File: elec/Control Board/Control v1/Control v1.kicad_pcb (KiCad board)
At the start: 2 copper layers, 126.3 x 160 mm, 175 parts, among them J10 Conn_02x12_Odd_Even, J103 Screw_Terminal_01x02, J106 Conn_01x04, J107 Conn_01x07, J11 Screw_Terminal_01x02, J111 Conn_01x08, J15 DB25_Female_MountingHoles, J16 Conn_01x04, J17 Conn_01x05, J18 Conn_01x04, J19 Conn_01x07, J2 DB9_Female_MountingHoles, J20 Screw_Terminal_01x02, J201 0.100_2Pin, J202 Conn_01x04, J21 Conn_01x04_Pin, J23 0.100_2Pin, J24 0.100_2Pin, J25 Conn_01x04, J3 Conn_01x08, J301 RJ12_6P6C_HORZ, J302 0.100_2Pin, J4 Conn_01x08, J5 Conn_01x08, J6 Conn_01x08, J7 Conn_01x08, J8 Conn_02x18_Odd_Even, J9 Conn_01x10_MountingPin, Q1 BSS138, Q10 BSS138, Q2 NCE01P30K, Q201 BSS138, Q202 BSS138, Q3 BSS138, Q301 BSS138, Q302 BSS138, Q303 BSS138, Q304 BSS138, Q4 BSS138, Q5 BSS138, Q6 BSS138, Q7 BSS138, Q8 BSS138, Q9 BSS138, SW101 SW_DIP_x08

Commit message: Add footrpint to Max31850 module.
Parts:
- removed J10: Conn_02x12_Odd_Even, Connector_PinHeader_2.00mm:PinHeader_2x12_P2.00mm_Vertical
- removed J301: RJ12_6P6C_HORZ, PubInv_PCB:RJ12_Amphenol_54601
- removed R102: DNI, Resistor_SMD:R_0603_1608Metric_Pad0.98x0.95mm_HandSolder
- removed SW101: SW_DIP_x08, PubInv_PCB:SMDIP-16_L11.39_W6.7mm
- added D2: DNI, Diode_SMD:D_MiniMELF, F.Cu at (70.0, 63.6)
- added J14: Conn_01x04, Connector_PinHeader_2.54mm:PinHeader_1x04_P2.54mm_Vertical, F.Cu at (61.2, 62.5)
- added J15: Conn_01x05, Connector_PinHeader_2.54mm:PinHeader_1x05_P2.54mm_Vertical, F.Cu at (75.8, 78.4)
- added J2: Conn_01x08, Connector_PinSocket_2.54mm:PinSocket_1x08_P2.54mm_Vertical, F.Cu at (159.0, 88.9)
- added J22: Conn_01x04, Connector_PinHeader_2.54mm:PinHeader_1x04_P2.54mm_Vertical, F.Cu at (43.4, 127.0)
- added JP1: Breakout, PubInv_KiCad_PCB:Adafruit_MAX31850K_Module, F.Cu at (222.5, 44.5)
- added JP2: Breakout, PubInv_KiCad_PCB:Adafruit_MAX31850K_Module, F.Cu at (222.5, 66.4)
- added JP3: Breakout, PubInv_KiCad_PCB:Adafruit_MAX31850K_Module, F.Cu at (222.5, 88.4)
- added JP6: SolderJumper_3_Bridged12, Jumper:SolderJumper-3_P1.3mm_Bridged12_RoundedPad1.0x1.5mm, F.Cu at (194.3, 34.9)
- added JP7: SolderJumper_3_Bridged12, Jumper:SolderJumper-3_P1.3mm_Bridged12_RoundedPad1.0x1.5mm, F.Cu at (194.3, 38.8)
- added JP8: SolderJumper_3_Bridged12, Jumper:SolderJumper-3_P1.3mm_Bridged12_RoundedPad1.0x1.5mm, F.Cu at (194.3, 42.6)
- added JP9: SolderJumper_3_Bridged12, Jumper:SolderJumper-3_P1.3mm_Bridged12_RoundedPad1.0x1.5mm, F.Cu at (194.9, 49.0)
- added R11: DNI, Resistor_SMD:R_0603_1608Metric_Pad0.98x0.95mm_HandSolder, F.Cu at (49.5, 91.0)
- added R15: 1K, Resistor_SMD:R_0603_1608Metric_Pad0.98x0.95mm_HandSolder, F.Cu at (65.6, 86.8)
- added R17: 1K, Resistor_SMD:R_0603_1608Metric_Pad0.98x0.95mm_HandSolder, F.Cu at (74.3, 85.6)
- added R51: 39R, Resistor_SMD:R_0603_1608Metric_Pad0.98x0.95mm_HandSolder, F.Cu at (22.7, 121.5)
- added R52: 1R, Resistor_SMD:R_0603_1608Metric_Pad0.98x0.95mm_HandSolder, F.Cu at (22.7, 124.0)
- added R53: DNI, Resistor_SMD:R_0603_1608Metric_Pad0.98x0.95mm_HandSolder, F.Cu at (22.7, 126.5)
- added R54: DNI, Resistor_SMD:R_0603_1608Metric_Pad0.98x0.95mm_HandSolder, F.Cu at (22.7, 129.0)
- added TP10: +VccMAX31850_1, TestPoint:TestPoint_Loop_D2.54mm_Drill1.5mm_Beaded, F.Cu at (245.1, 27.4)
- added TP9: SDA_5V, TestPoint:TestPoint_Loop_D2.54mm_Drill1.5mm_Beaded, F.Cu at (27.4, 122.7)
- J17: value Conn_01x05 -> Conn_01x07; footprint Connector_PinHeader_2.54mm:PinHeader_1x05_P2.54mm_Vertical -> Connector_PinHeader_2.54mm:PinHeader_1x07_P2.54mm_Vertical
- J18: value Conn_01x04 -> Conn_01x04_Pin
- J19: value Conn_01x07 -> RJ12_6P6C_HORZ; footprint Connector_PinHeader_2.54mm:PinHeader_1x07_P2.54mm_Vertical -> PubInv_KiCad_PCB:RJ12_Amphenol_54601
- J20: value Screw_Terminal_01x02 -> 0.100_2Pin; footprint TerminalBlock_MetzConnect:TerminalBlock_MetzConnect_Type073_RT02602HBLU_1x02_P5.08mm_Horizontal -> Connector_PinHeader_2.54mm:PinHeader_1x02_P2.54mm_Vertical
- J21: value Conn_01x04_Pin -> 0.100_2Pin; footprint Connector_PinHeader_2.54mm:PinHeader_1x04_P2.54mm_Vertical -> Connector_PinHeader_2.54mm:PinHeader_1x02_P2.54mm_Vertical
- J4: footprint Connector_PinSocket_2.54mm:PinSocket_1x08_P2.54mm_Vertical -> Connector_PinHeader_2.54mm:PinHeader_1x08_P2.54mm_Vertical
- J7: value Conn_01x08 -> Conn_02x18_Odd_Even; footprint Connector_PinSocket_2.54mm:PinSocket_1x08_P2.54mm_Vertical -> Connector_PinSocket_2.54mm:PinSocket_2x18_P2.54mm_Vertical
- J8: value Conn_02x18_Odd_Even -> Conn_01x10_MountingPin; footprint Connector_PinSocket_2.54mm:PinSocket_2x18_P2.54mm_Vertical -> Connector_PinSocket_2.54mm:PinSocket_1x10_P2.54mm_Vertical
- J9: value Conn_01x10_MountingPin -> Conn_02x12_Odd_Even; footprint Connector_PinSocket_2.54mm:PinSocket_1x10_P2.54mm_Vertical -> Connector_PinHeader_2.00mm:PinHeader_2x12_P2.00mm_Vertical
- R10, R27, R4, R5: value DNI -> 1R0
- R12: value 1K -> 1R0
- R13, R22, R32: value 1K -> DNI
- R18: value 10K -> 10k
- R19: value 1K -> 10k
- R20: value 1K -> 10K
- R21, R36: value 10K -> 1K
- R23: value 1R0 -> 10K
- R24, R41: value 1R -> 1K
- R25, R48: value 1R -> 10K
- R26, R6, R7, R8: value DNI -> 1K
- R28, R38: value DNI -> 1R
- R29: value 1K -> 1R
- R31, R39, R42: value 10K -> DNI
- R34: value 1R -> DNI
- R35, R49: value DNI -> 10K
- R45: value 10K -> 1R
- R46, R47: value 39R -> 10K
- R50: value DNI -> 39R
- R9: value 1R0 -> 1K
- TP1: value ControllerVCC -> +VccMAX31850
- TP2: value CPIO -> ControllerVCC
- TP3: value SCK -> CPIO
- TP4: value COPI -> SCK
- TP5: value nCS -> COPI
- TP6: value I2C_VCC -> nCS
- TP7: value SCL_5V -> I2C_VCC
- TP8: value SDA_5V -> SCL_5V
- moved D1 172.5 mm to (69.6, 83.2)
- moved R23 170.4 mm to (77.9, 58.0)
- moved R22 166.8 mm to (82.7, 91.0)
- moved Q1 166.8 mm to (70.4, 88.2)
- moved R25 165.0 mm to (84.7, 60.4), turned to 180 degrees
- moved R24 165.0 mm to (84.9, 57.4)
- moved J19 159.2 mm to (51.0, 105.0), turned to -90 degrees
- moved J11 153.7 mm to (91.1, 26.6)
- moved Q3 150.7 mm to (84.6, 52.2)
- moved R12 148.5 mm to (53.2, 85.8)
- moved Q2 142.7 mm to (76.8, 52.3)
- moved R13 136.5 mm to (65.7, 89.6), turned to 180 degrees
- moved R7 132.8 mm to (197.6, 71.0)
- moved R9 131.1 mm to (190.8, 66.2)
- moved R6 130.0 mm to (194.9, 67.0)
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- renumbered J2 to J1, J15 to J13
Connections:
- A1 pad A1: Net-(J6-Pin_2) -> Net-(J5-Pin_2)
- A1 pad A10: Net-(J4-Pin_3) -> Net-(J3-Pin_3)
- A1 pad A11: Net-(J4-Pin_4) -> Net-(J3-Pin_4)
- A1 pad A2: Net-(J6-Pin_3) -> Net-(J5-Pin_3)
- A1 pad A3: Net-(J6-Pin_4) -> Net-(J5-Pin_4)
- A1 pad A4: Net-(J6-Pin_5) -> Net-(J5-Pin_5)
- A1 pad A5: Net-(J6-Pin_6) -> Net-(J5-Pin_6)
- A1 pad A6: Net-(J6-Pin_7) -> Net-(J5-Pin_7)
- A1 pad A7: Net-(J6-Pin_8) -> Net-(J5-Pin_8)
- A1 pad A8: Net-(J4-Pin_1) -> Net-(J3-Pin_1)
- A1 pad A9: Net-(J4-Pin_2) -> Net-(J3-Pin_2)
- A1 pad D11: Net-(J9-Pin_7) -> Net-(J8-Pin_7)
- A1 pad D12: Net-(J9-Pin_6) -> Net-(J8-Pin_6)
- A1 pad D13: Net-(J9-Pin_5) -> Net-(J8-Pin_5)
- A1 pad D2: Net-(J7-Pin_3) -> Net-(J6-Pin_3)
- A1 pad D22: Net-(J8-Pin_3) -> BLOWER_ENABLE
- A1 pad D24: Net-(J8-Pin_5) -> Net-(J7-Pin_5)
- A1 pad D26: Net-(J8-Pin_7) -> Net-(J7-Pin_7)
- A1 pad D28: Net-(J8-Pin_9) -> Net-(J7-Pin_9)
- A1 pad D3: Net-(J7-Pin_4) -> Net-(J6-Pin_4)
- A1 pad D30: Net-(J8-Pin_11) -> Net-(J7-Pin_11)
- A1 pad D32: Net-(J8-Pin_13) -> D32
- A1 pad D34: Net-(J8-Pin_15) -> Net-(J7-Pin_15)
- A1 pad D36: Net-(J8-Pin_17) -> Net-(J7-Pin_17)
- A1 pad D38: Net-(J8-Pin_19) -> Net-(J7-Pin_19)
- A1 pad D40: Net-(J8-Pin_21) -> Net-(J7-Pin_21)
- A1 pad D42: Net-(J8-Pin_23) -> Net-(J7-Pin_23)
- A1 pad D44: Net-(J8-Pin_25) -> Net-(J7-Pin_25)
- A1 pad D46: Net-(J8-Pin_27) -> Net-(J7-Pin_27)
- A1 pad D48: Net-(J8-Pin_29) -> Net-(J7-Pin_29)
- A1 pad D5: Net-(J7-Pin_6) -> Net-(J6-Pin_6)
- A1 pad D50: Net-(J8-Pin_31) -> Net-(J7-Pin_31)
- A1 pad D53: Net-(J8-Pin_34) -> Net-(J7-Pin_34)
- A1 pad D6: Net-(J7-Pin_7) -> Net-(J6-Pin_7)
- A1 pad D7: Net-(J7-Pin_8) -> Net-(J6-Pin_8)
- A1 pad D8: Net-(J9-Pin_10) -> Net-(J8-Pin_10)
- A1 pad VIN: Net-(J5-Pin_1) -> Net-(J4-Pin_1)
- J11 pad 1: unconnected-(J11-Pin_1-Pad1) -> +24V
- J11 pad 2: +24V -> GND
- J13 pad 13: Net-(J18-Pin_4) -> Net-(J16-Pin_4)
- J13 pad 18: Net-(J15-P18) -> Net-(J13-P18)
- J13 pad 19: Net-(J15-P19) -> Net-(J13-P19)
- J13 pad 20: Net-(J15-P20) -> Net-(J13-P20)
- J13 pad 21: Net-(J15-P21) -> Net-(J13-P21)
- J13 pad 22: Net-(J15-P22) -> Net-(J13-P22)
- J13 pad 23: Net-(J15-P23) -> Net-(J13-P23)
- J13 pad 24: Net-(J15-P24) -> Net-(J13-P24)
- J13 pad 25: Net-(J15-P25) -> Net-(J13-P25)
- J16 pad 1: /Blower controller/TachFan1 -> GND
- J16 pad 2: /Blower controller/TachFan2 -> unconnected-(J16-Pin_2-Pad2)
- J16 pad 3: /Blower controller/TachFan3 -> Net-(J13-P25)
- J16 pad 4: /Blower controller/TachFan4 -> Net-(J16-Pin_4)
- J17 pad 1: /Blower controller/PWMFan1 -> Net-(J13-P18)
- J17 pad 2: /Blower controller/PWMFan2 -> Net-(J13-P19)
- J17 pad 3: /Blower controller/PWMFan3 -> Net-(J13-P20)
- J17 pad 4: /Blower controller/PWMFan4 -> Net-(J13-P21)
- J17 pad 5: Net-(J17-Pin_5) -> Net-(J13-P22)
- J18 pad 2: +3.3V -> /Blower controller/Switched_Fan_Power
- J18 pad 3: Net-(J15-P25) -> /Blower controller/TachFan1
- J18 pad 4: Net-(J18-Pin_4) -> Net-(D1-K)
- J19 pad 1: Net-(J15-P18) -> /SPI_ControllerLevel_Shifter/nCS
- J19 pad 2: Net-(J15-P19) -> /SPI_ControllerLevel_Shifter/COPI
- J19 pad 3: Net-(J15-P20) -> GND
- J19 pad 4: Net-(J15-P21) -> /SPI_ControllerLevel_Shifter/C_SCK
- J19 pad 5: Net-(J15-P22) -> /SPI_ControllerLevel_Shifter/ControllerVcc
- J19 pad 6: Net-(J15-P23) -> /SPI_ControllerLevel_Shifter/CIPO
- J20 pad 1: GND -> /SPI_ControllerLevel_Shifter/ControllerVcc
- J20 pad 2: Net-(J17-Pin_5) -> +12V
- J21 pad 1: GND -> /I2C_LevelShift/I2C_VCC
- J21 pad 2: /Blower controller/Switched_Fan_Power -> /I2C_LevelShift/+12forSPIPeripherial
- J3 pad 1: Net-(A1-D14/TX3) -> Net-(J3-Pin_1)
- J3 pad 2: Net-(A1-D15/RX3) -> Net-(J3-Pin_2)
- J3 pad 3: Net-(A1-D16/TX2) -> Net-(J3-Pin_3)
- J3 pad 4: Net-(A1-D17/RX2) -> Net-(J3-Pin_4)
- J3 pad 5: /D_PSU_TX -> DAC0
- J3 pad 6: /D_PSU_RX -> DAC1
- J3 pad 7: D23 -> CANR
- J3 pad 8: D22 -> CANT
- J4 pad 2: Net-(J4-Pin_2) -> GND
- J4 pad 3: Net-(J4-Pin_3) -> GND
- J4 pad 4: Net-(J4-Pin_4) -> +5V
- J4 pad 5: DAC0 -> +3.3V
- J4 pad 6: DAC1 -> Net-(A1-RESET)
- J4 pad 7: CANR -> Net-(A1-IOREF)
- J4 pad 8: CANT -> unconnected-(J4-Pin_8-Pad8)
- J5 pad 1: Net-(J5-Pin_1) -> BLOWER_TACH
- J5 pad 2: GND -> Net-(J5-Pin_2)
- J5 pad 3: GND -> Net-(J5-Pin_3)
- J5 pad 4: +5V -> Net-(J5-Pin_4)
- J5 pad 5: +3.3V -> Net-(J5-Pin_5)
- J5 pad 6: Net-(A1-RESET) -> Net-(J5-Pin_6)
- J5 pad 7: Net-(A1-IOREF) -> Net-(J5-Pin_7)
- J5 pad 8: unconnected-(J5-Pin_8-Pad8) -> Net-(J5-Pin_8)
- J6 pad 1: BLOWER_TACH -> D0
- J6 pad 2: Net-(J6-Pin_2) -> D1
- J6 pad 5: Net-(J6-Pin_5) -> ONE_WIRE_TC
- J7 pad 1: D0 -> 5V3
- J7 pad 2: D1 -> 5V4
- J7 pad 3: Net-(J7-Pin_3) -> BLOWER_ENABLE
- J7 pad 4: Net-(J7-Pin_4) -> D23
- J7 pad 5: ONE_WIRE_TC -> Net-(J7-Pin_5)
- J7 pad 6: Net-(J7-Pin_6) -> D25
- J7 pad 8: Net-(J7-Pin_8) -> D27
- J8 pad 1: 5V3 -> SCL1
- J8 pad 10: D29 -> Net-(J8-Pin_10)
- J8 pad 2: 5V4 -> SDA1
- J8 pad 3: Net-(J8-Pin_3) -> AREF
- J8 pad 4: D23 -> GND
- J8 pad 6: D25 -> Net-(J8-Pin_6)
- J8 pad 8: D27 -> Net-(A1-D10_CS0)
- J8 pad 9: Net-(J8-Pin_9) -> BLOWER_PWM
- J9 pad 1: SCL1 -> /VO+
- J9 pad 10: Net-(J9-Pin_10) -> /EN-
- J9 pad 2: SDA1 -> /VS+
- J9 pad 3: AREF -> /VO-
- J9 pad 4: GND -> /VS-
- J9 pad 5: Net-(J9-Pin_5) -> GND
- J9 pad 6: Net-(J9-Pin_6) -> /POK
- J9 pad 7: Net-(J9-Pin_7) -> /VSET
- J9 pad 8: Net-(A1-D10_CS0) -> /PAR
- J9 pad 9: BLOWER_PWM -> GND
- Q2 pad 3: Net-(Q2-S) -> +24V
- Q5 pad 2: /SPI_ControllerLevel_Shifter/COPI_nCS -> D32
- R1 pad 2: BLOWER_???? -> BLOWER_ENABLE
- R10 pad 1: /Blower controller/nFAN1_PWM -> +5V
- R10 pad 2: Net-(D1-K) -> /Thermocouple Amplifier with 1-Wire Breakout Board - MAX31850K/+VccMAX31850
- R12 pad 1: Net-(D1-K) -> /Blower controller/PWMFan1
- R12 pad 2: /Blower controller/+5VFan -> Net-(D1-K)
- R13 pad 1: /Blower controller/TachFan1 -> /Blower controller/nFAN1_PWM
- R13 pad 2: /Blower controller/+3.3VFan -> Net-(D1-K)
- R16 pad 1: /Blower controller/FAN1_FG -> /Blower controller/TachFan1
- R16 pad 2: /Blower controller/TachFan1 -> /Blower controller/+3.3VFan
- R18 pad 1: Net-(R14-Pad2) -> +24V
- R18 pad 2: Net-(Q3-D) -> Net-(R18-Pad2)
- R19 pad 1: Net-(Q1-G) -> Net-(Q2-G)
- R19 pad 2: /Blower controller/nFAN1_PWM -> Net-(Q3-D)
- R20 pad 1: Net-(Q3-G) -> /Blower controller/+3.3VFan
- R20 pad 2: /Blower controller/FAN_POWER -> /Blower controller/nFAN1_PWM
- R21 pad 1: /Blower controller/FAN_POWER -> /Blower controller/FAN1_FG
- R21 pad 2: GND -> /Blower controller/TachFan1
- R22 pad 1: /SSR Interface/Heater -> /Blower controller/FAN1_FG
- R22 pad 2: Net-(Q4-G) -> GND
- R23 pad 1: Net-(Q4-D) -> Net-(R18-Pad2)
- R23 pad 2: /SSR Interface/Heater_SSR_Low -> Net-(Q3-D)
- R24 pad 1: /SPI_ControllerLevel_Shifter/ControllerVcc -> Net-(Q3-G)
- R24 pad 2: +12V -> /Blower controller/FAN_POWER
- R25 pad 1: +5V -> /Blower controller/FAN_POWER
- R25 pad 2: /SPI_ControllerLevel_Shifter/+5VLocal -> GND
- R26 pad 1: /SPI_ControllerLevel_Shifter/CIPO -> /SSR Interface/Heater
- R26 pad 2: CIPO -> Net-(Q4-G)
- R27 pad 1: /SPI_ControllerLevel_Shifter/C_SCK -> Net-(Q4-D)
- R27 pad 2: SPI_SCK -> /SSR Interface/Heater_SSR_Low
- R28 pad 1: /SPI_ControllerLevel_Shifter/COPI -> /SPI_ControllerLevel_Shifter/ControllerVcc
- R28 pad 2: COPI -> +12V
- R29 pad 1: /SPI_ControllerLevel_Shifter/+5VLocal -> +5V
- R29 pad 2: /SPI_ControllerLevel_Shifter/nCS -> /SPI_ControllerLevel_Shifter/+5VLocal
- R30 pad 1: /SPI_ControllerLevel_Shifter/nCS -> /SPI_ControllerLevel_Shifter/CIPO
- R30 pad 2: /SPI_ControllerLevel_Shifter/COPI_nCS -> CIPO
- R31 pad 1: /SPI_ControllerLevel_Shifter/+5VLocal -> /SPI_ControllerLevel_Shifter/C_SCK
- R31 pad 2: /SPI_ControllerLevel_Shifter/CIPO -> SPI_SCK
- R32 pad 1: /SPI_ControllerLevel_Shifter/+5VLocal -> /SPI_ControllerLevel_Shifter/COPI
- R32 pad 2: /SPI_ControllerLevel_Shifter/C_SCK -> COPI
- R33 pad 2: /SPI_ControllerLevel_Shifter/COPI -> /SPI_ControllerLevel_Shifter/nCS
- R34 pad 1: +3.3V -> /SPI_ControllerLevel_Shifter/nCS
- R34 pad 2: /SPI_ControllerLevel_Shifter/+3V3Local -> D32
- R35 pad 1: Net-(R35-Pad1) -> /SPI_ControllerLevel_Shifter/+5VLocal
- R35 pad 2: CIPO -> /SPI_ControllerLevel_Shifter/CIPO
- R36 pad 1: /SPI_ControllerLevel_Shifter/+3V3Local -> /SPI_ControllerLevel_Shifter/+5VLocal
- R36 pad 2: /SPI_ControllerLevel_Shifter/COPI_nCS -> /SPI_ControllerLevel_Shifter/C_SCK
- R37 pad 1: /SPI_ControllerLevel_Shifter/+3V3Local -> /SPI_ControllerLevel_Shifter/+5VLocal
- R37 pad 2: CIPO -> /SPI_ControllerLevel_Shifter/COPI
- R38 pad 1: GND -> +3.3V
- R38 pad 2: Net-(R35-Pad1) -> /SPI_ControllerLevel_Shifter/+3V3Local
- R39 pad 1: /SPI_ControllerLevel_Shifter/+3V3Local -> Net-(R39-Pad1)
- R39 pad 2: SPI_SCK -> CIPO
- R4 pad 1: +3.3V -> SCL
- R4 pad 2: /Blower controller/TachFan4 -> Net-(J9-Pin_20)
- R40 pad 2: COPI -> D32
- R41 pad 1: /I2C_LevelShift/+3V3LevelShift -> /SPI_ControllerLevel_Shifter/+3V3Local
- R41 pad 2: /I2C_LevelShift/+3V3Local -> CIPO
- R42 pad 1: /I2C_LevelShift/+3V3Local -> GND
- R42 pad 2: SCL -> Net-(R39-Pad1)
- R43 pad 1: /I2C_LevelShift/+3V3Local -> /SPI_ControllerLevel_Shifter/+3V3Local
- R43 pad 2: SDA -> SPI_SCK
- R44 pad 1: /I2C_LevelShift/+5VLocal -> /SPI_ControllerLevel_Shifter/+3V3Local
- R44 pad 2: Net-(Q9-D) -> COPI
- R45 pad 1: /I2C_LevelShift/+5VLocal -> /I2C_LevelShift/+3V3LevelShift
- R45 pad 2: Net-(Q10-D) -> /I2C_LevelShift/+3V3Local
- R46 pad 1: /I2C_LevelShift/SCL_5V -> /I2C_LevelShift/+3V3Local
- R46 pad 2: Net-(Q9-D) -> SCL
- R47 pad 1: /I2C_LevelShift/SDA_5V -> /I2C_LevelShift/+3V3Local
- R47 pad 2: Net-(Q10-D) -> SDA
- R48 pad 2: /I2C_LevelShift/+5LevelShift -> Net-(Q9-D)
- R49 pad 1: /I2C_LevelShift/I2C_VCC -> /I2C_LevelShift/+5VLocal
- R49 pad 2: /I2C_LevelShift/+5LevelShift -> Net-(Q10-D)
- R5 pad 1: /Blower controller/TachFan1 -> Net-(J9-Pin_19)
- R5 pad 2: GND -> SDA
- R50 pad 1: /I2C_LevelShift/I2C_VCC -> /I2C_LevelShift/SCL_5V
- R50 pad 2: /I2C_LevelShift/+12forSPIPeripherial -> Net-(Q9-D)
- R6 pad 1: +3.3V -> Net-(JP9-C)
- R6 pad 2: /Blower controller/TachFan3 -> Net-(JP1-Pad2)
- R7 pad 1: +3.3V -> Net-(JP6-C)
- R7 pad 2: /Blower controller/TachFan2 -> Net-(JP1-Pad3)
- R8 pad 1: +3.3V -> Net-(JP7-C)
- R8 pad 2: /Blower controller/TachFan1 -> Net-(JP1-Pad4)
- R9 pad 1: /Blower controller/PWMFan1 -> Net-(JP8-C)
- R9 pad 2: Net-(D1-K) -> Net-(JP1-Pad5)
- TP1 pad 1: /SPI_ControllerLevel_Shifter/ControllerVcc -> /Thermocouple Amplifier with 1-Wire Breakout Board - MAX31850K/+VccMAX31850
- TP2 pad 1: /SPI_ControllerLevel_Shifter/CIPO -> /SPI_ControllerLevel_Shifter/ControllerVcc
- TP3 pad 1: /SPI_ControllerLevel_Shifter/C_SCK -> /SPI_ControllerLevel_Shifter/CIPO
- TP4 pad 1: /SPI_ControllerLevel_Shifter/COPI -> /SPI_ControllerLevel_Shifter/C_SCK
- TP5 pad 1: /SPI_ControllerLevel_Shifter/nCS -> /SPI_ControllerLevel_Shifter/COPI
- TP6 pad 1: /I2C_LevelShift/I2C_VCC -> /SPI_ControllerLevel_Shifter/nCS
- TP7 pad 1: /I2C_LevelShift/SCL_5V -> /I2C_LevelShift/I2C_VCC
- TP8 pad 1: /I2C_LevelShift/SDA_5V -> /I2C_LevelShift/SCL_5V

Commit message: Add footprints for thermoucouple modules to schematic and PCB.  This commit does NOT capture the library changes.
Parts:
- added JP10: MAX31855, PubInv_KiCad_PCB:Adafruit_MAX31855_Module, F.Cu at (308.8, 112.8)
- added JP11: MAX31865, PubInv_KiCad_PCB:Adafruit_MAX31865_Module, F.Cu at (262.7, 87.0)
- added JP12: MAX31865, PubInv_KiCad_PCB:Adafruit_MAX31865_Module, F.Cu at (290.2, 87.0)
- added JP13: MAX31865, PubInv_KiCad_PCB:Adafruit_MAX31865_Module, F.Cu at (317.7, 87.0)
- added JP8: MAX31855, PubInv_KiCad_PCB:Adafruit_MAX31855_Module, F.Cu at (264.0, 112.8)
- added JP9: MAX31855, PubInv_KiCad_PCB:Adafruit_MAX31855_Module, F.Cu at (286.4, 112.8)
- JP5: renamed from JP1; value Breakout -> MAX31850K
- JP6: renamed from JP2; value Breakout -> MAX31850K
- JP7: renamed from JP3; value Breakout -> MAX31850K
- moved TP10 31.6 mm to (37.4, 152.7)
- moved C2 31.6 mm to (61.9, 84.4)
- moved C301 31.6 mm to (65.3, 146.3)
- moved C302 31.6 mm to (65.3, 141.3)
- moved C303 31.6 mm to (65.3, 137.3)
- moved C304 31.6 mm to (65.3, 133.3)
- moved C4 31.6 mm to (61.6, 92.4)
- moved J14 31.6 mm to (71.2, 92.5)
- moved J16 31.6 mm to (98.2, 74.5)
- moved JP3 31.6 mm to (204.3, 64.9)
- moved Q2 31.6 mm to (86.8, 82.3)
- moved Q301 31.6 mm to (77.3, 132.3)
- moved Q302 31.6 mm to (77.3, 153.3)
- moved Q303 31.6 mm to (77.3, 146.3)
- moved Q304 31.6 mm to (77.3, 139.3)
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- renumbered JP8 to JP1, JP7 to JP2, JP6 to JP3, JP9 to JP4, R9 to R10, R10 to R7, R7 to R8, R8 to R9, TP9 to TP10, TP10 to TP2, TP2 to TP3, TP3 to TP4, TP4 to TP5, TP5 to TP6, TP6 to TP7, TP7 to TP8, TP8 to TP9

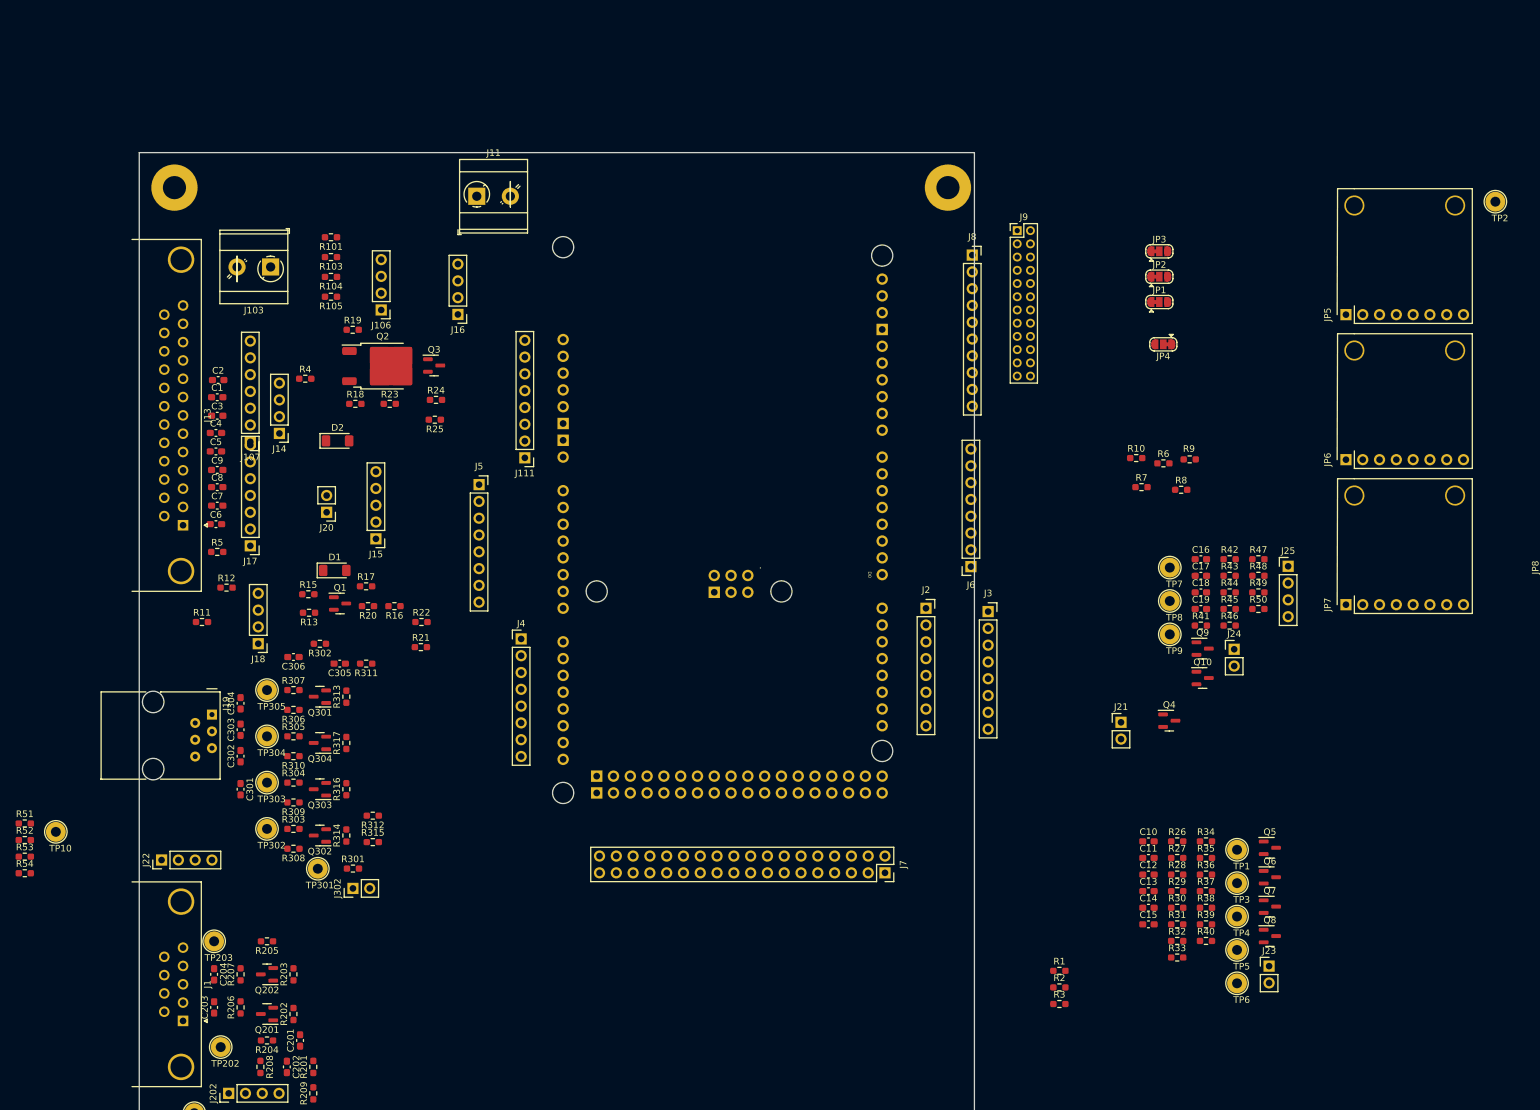
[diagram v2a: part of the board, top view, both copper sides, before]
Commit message: Fix mounting holes for thermocouple.
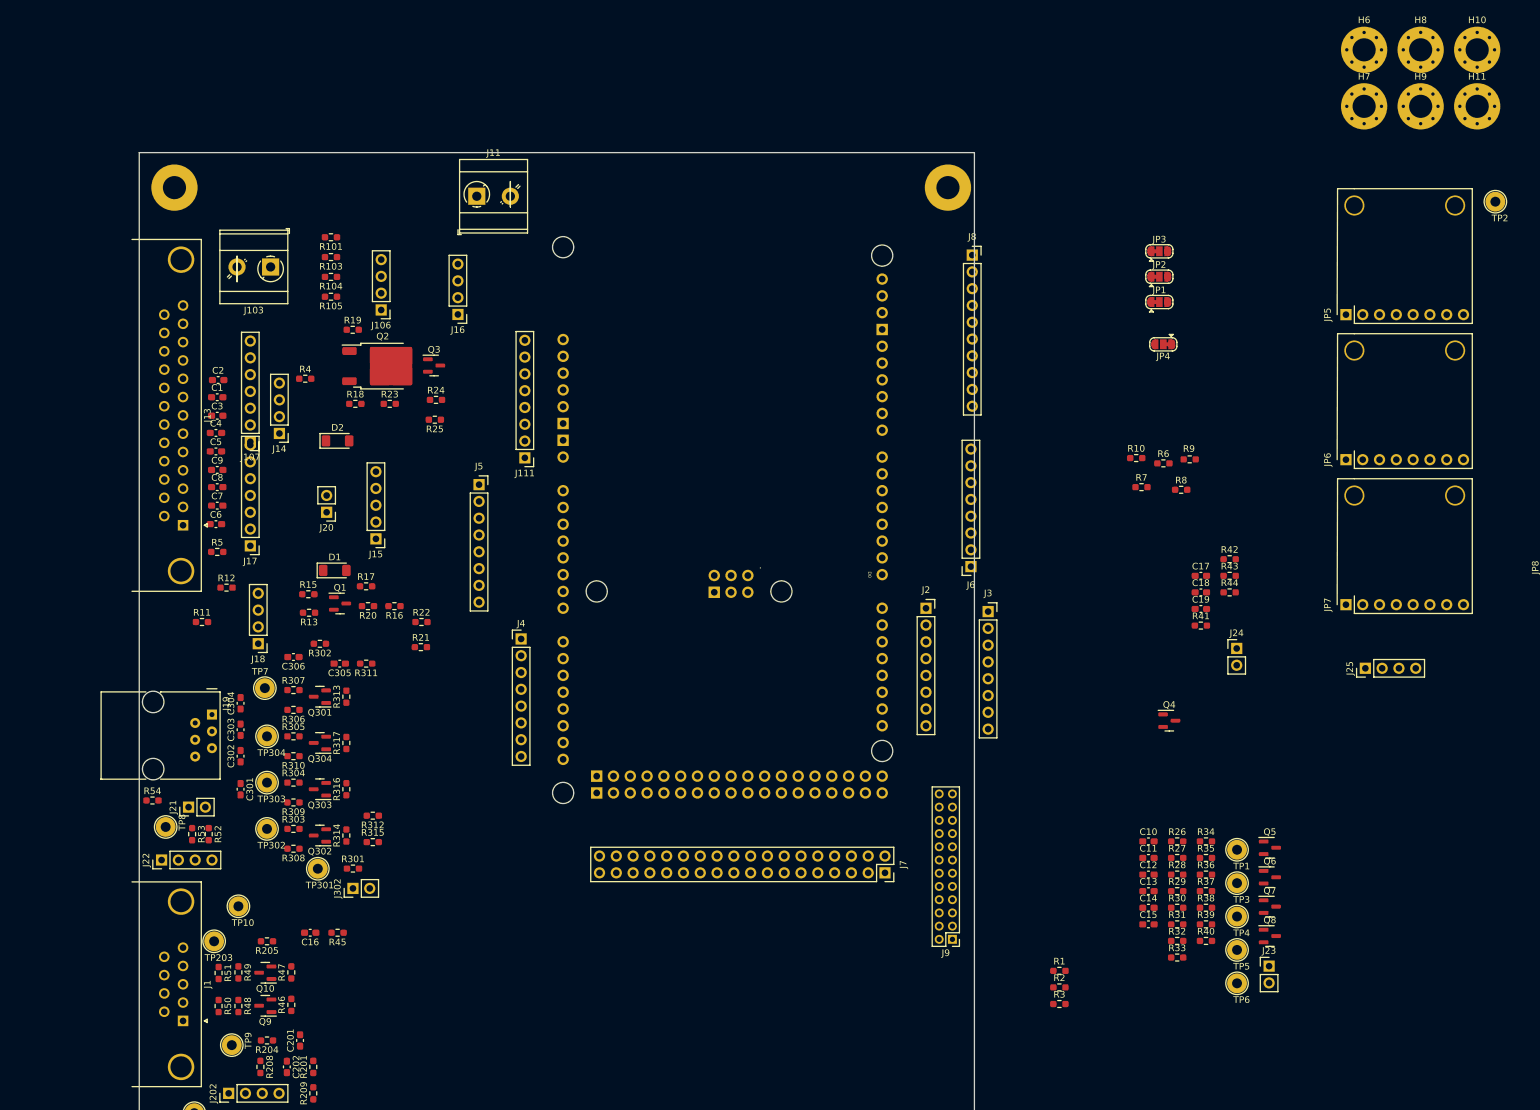
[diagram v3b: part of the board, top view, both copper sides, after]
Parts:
- removed C203, C204: 39PF, Capacitor_SMD:C_0603_1608Metric_Pad1.08x0.95mm_HandSolder
- removed Q201, Q202: BSS138, Package_TO_SOT_SMD:SOT-23
- removed R202, R203: 10K, Resistor_SMD:R_0603_1608Metric_Pad0.98x0.95mm_HandSolder
- removed R206, R207: 39R, Resistor_SMD:R_0603_1608Metric_Pad0.98x0.95mm_HandSolder
- removed TP202: SCL_5V, TestPoint:TestPoint_Loop_D2.54mm_Drill1.5mm_Beaded
- removed TP305: nCS, TestPoint:TestPoint_Loop_D2.54mm_Drill1.5mm_Beaded
- added H10: MountingHole_Pad_3.5mm, PubInv_KiCad_PCB:MountingHole_3.5mm_Pad_Via, F.Cu at (252.4, 34.5)
- added H11: MountingHole_Pad_3.5mm, PubInv_KiCad_PCB:MountingHole_3.5mm_Pad_Via, F.Cu at (252.4, 43.0)
- added H6: MountingHole_Pad_3.5mm, PubInv_KiCad_PCB:MountingHole_3.5mm_Pad_Via, F.Cu at (235.3, 34.5)
- added H7: MountingHole_Pad_3.5mm, PubInv_KiCad_PCB:MountingHole_3.5mm_Pad_Via, F.Cu at (235.3, 43.0)
- added H8: MountingHole_Pad_3.5mm, PubInv_KiCad_PCB:MountingHole_3.5mm_Pad_Via, F.Cu at (243.8, 34.5)
- added H9: MountingHole_Pad_3.5mm, PubInv_KiCad_PCB:MountingHole_3.5mm_Pad_Via, F.Cu at (243.8, 43.0)
- moved R50 168.4 mm to (62.0, 179.1), turned to -90 degrees
- moved R48 167.4 mm to (65.0, 179.1), turned to -90 degrees
- moved R49 164.6 mm to (65.0, 174.0), turned to -90 degrees
- moved R47 159.1 mm to (73.0, 174.0), turned to 90 degrees
- moved TP8 155.7 mm to (54.0, 152.0), turned to 90 degrees
- moved TP9 154.9 mm to (64.0, 185.0), turned to 90 degrees
- moved R46 153.1 mm to (73.0, 178.9), turned to 90 degrees
- moved Q9 151.7 mm to (69.1, 179.1), turned to 180 degrees
- moved Q10 148.6 mm to (69.1, 174.1), turned to 180 degrees
- moved C16 146.1 mm to (75.9, 168.0), turned to 180 degrees
- moved R45 143.5 mm to (80.0, 168.0), turned to 180 degrees
- moved J21 141.6 mm to (57.5, 149.0), turned to 90 degrees
- moved TP7 138.1 mm to (69.0, 131.0), turned to 180 degrees
- moved J9 107.6 mm to (173.0, 169.0), turned to 180 degrees
- moved R51 37.0 mm to (62.0, 174.1), turned to -90 degrees
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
